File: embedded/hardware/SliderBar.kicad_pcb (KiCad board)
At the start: 2 copper layers, 101.6 x 25.4 mm, 35 parts, among them J1 USB_B_Mini, J2 MOTOR_OUT, J3 POT_IN, J4 DEBUG, U1 MIC5205-3.3YM5, U2 TB6612FNG, U3 MT3608, U4 STM32F072C8Tx

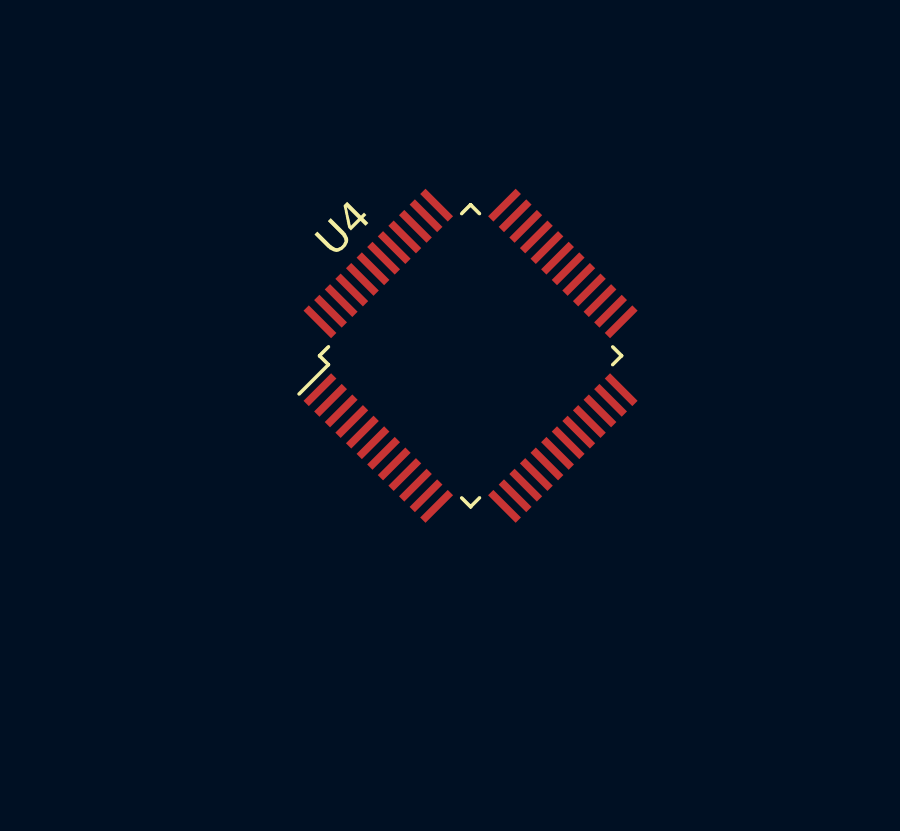
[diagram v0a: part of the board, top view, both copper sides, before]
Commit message: Rotated mcu
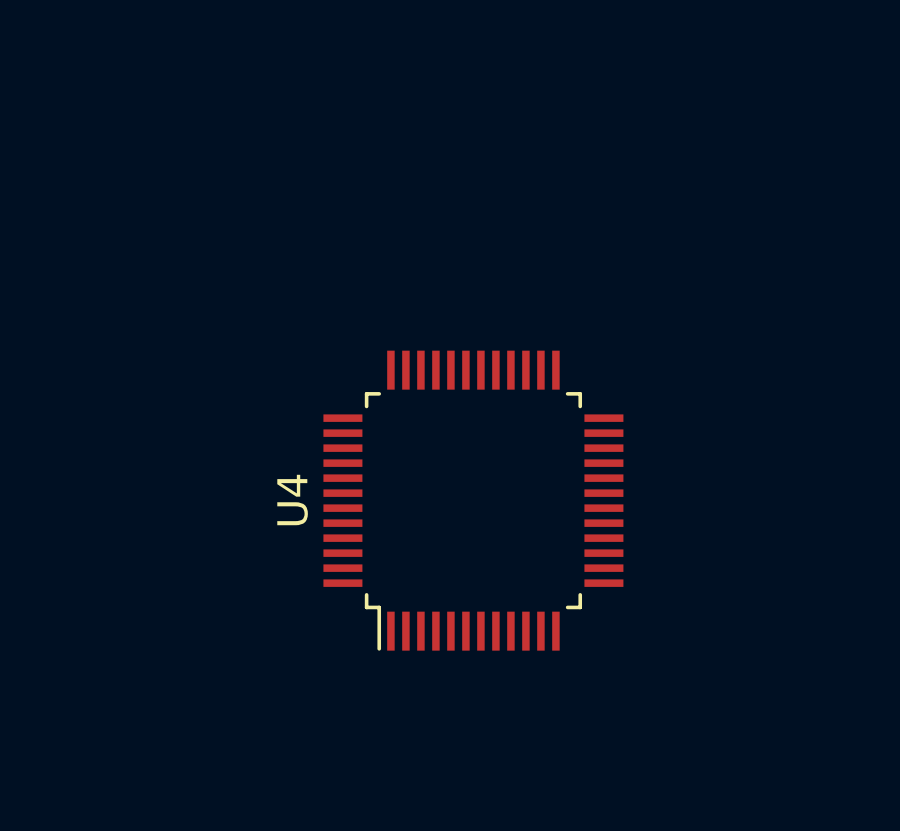
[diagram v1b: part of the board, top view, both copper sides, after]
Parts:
- moved U4 4.83 mm to (120.0, 62.2), turned to 90 degrees

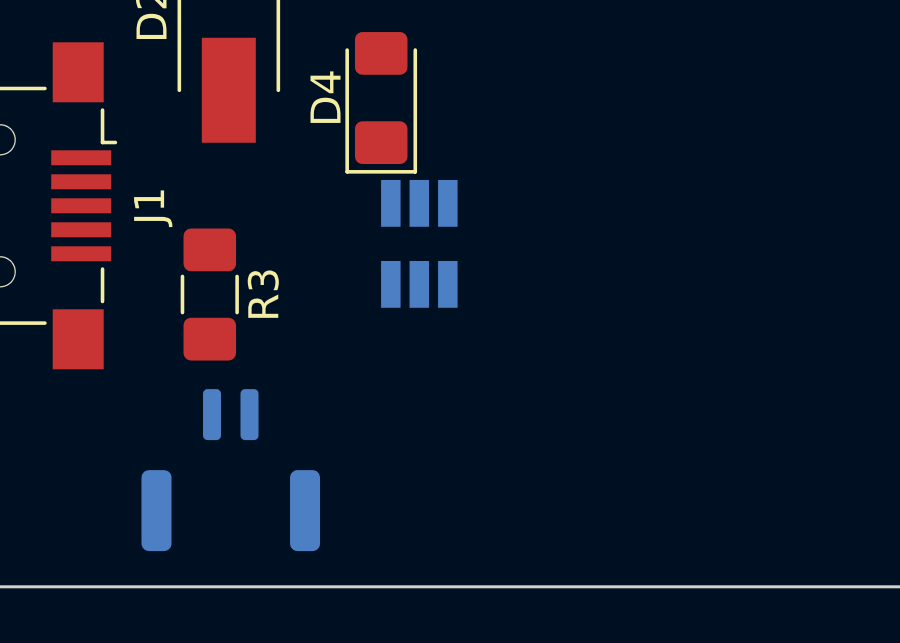
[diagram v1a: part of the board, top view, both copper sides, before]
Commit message: Add GND to power class
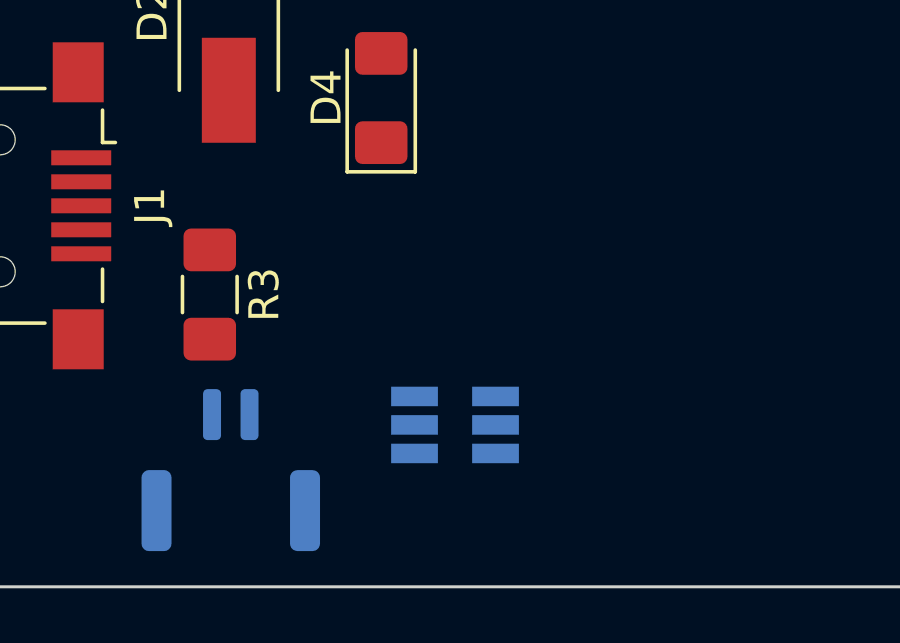
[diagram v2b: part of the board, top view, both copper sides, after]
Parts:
- moved U3 6.15 mm to (115.5, 103.8), turned to 0 degrees
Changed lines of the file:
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@@
     (uvia_drill 0.1)
     (add_net +3V3)
-    (add_net GND)
     (add_net MOT_IN_1)
     (add_net MOT_IN_2)
@@
     (add_net +10V)
     (add_net +5V)
+    (add_net GND)
     (add_net MOT_OUT_1)
     (add_net MOT_OUT_2)
@@
   )
   (module Package_TO_SOT_SMD:SOT-23-6_Handsoldering (layer B.Cu)
-    (at 114.3 97.79 90)
+    (at 115.49 103.825)
     (descr "6-pin SOT-23 package, Handsoldering")
     (tags "SOT-23-6 Handsoldering")
     (attr smd)
-    (fp_text reference U3 (at 0 2.9 90) (layer B.SilkS)
+    (fp_text reference U3 (at 0 2.9) (layer B.SilkS)
       (effects (font (size 1 1) (thickness 0.15)) (justify mirror))
     )
-    (fp_text value MT3608 (at 0 -2.9 90) (layer B.Fab)
+    (fp_text value MT3608 (at 0 -2.9) (layer B.Fab)
       (effects (font (size 1 1) (thickness 0.15)) (justify mirror))
     )
@@
     (fp_line (start 0.9 1.61) (end -2.05 1.61) (layer B.SilkS) (width 0.12))
     (fp_line (start -0.9 -1.61) (end 0.9 -1.61) (layer B.SilkS) (width 0.12))
-    (fp_text user %R (at 0 0) (layer B.Fab)
+    (fp_text user %R (at 0 0 -90) (layer B.Fab)
       (effects (font (size 0.5 0.5) (thickness 0.075)) (justify mirror))
     )
-    (pad 5 smd rect (at 1.35 0 90) (size 1.56 0.65) (layers B.Cu B.Paste B.Mask)
+    (pad 5 smd rect (at 1.35 0) (size 1.56 0.65) (layers B.Cu B.Paste B.Mask)
       (net 2 +5V))
-    (pad 6 smd rect (at 1.35 0.95 90) (size 1.56 0.65) (layers B.Cu B.Paste B.Mask))
-    (pad 4 smd rect (at 1.35 -0.95 90) (size 1.56 0.65) (layers B.Cu B.Paste B.Mask)
+    (pad 6 smd rect (at 1.35 0.95) (size 1.56 0.65) (layers B.Cu B.Paste B.Mask))
+    (pad 4 smd rect (at 1.35 -0.95) (size 1.56 0.65) (layers B.Cu B.Paste B.Mask)
       (net 2 +5V))
-    (pad 3 smd rect (at -1.35 -0.95 90) (size 1.56 0.65) (layers B.Cu B.Paste B.Mask)
+    (pad 3 smd rect (at -1.35 -0.95) (size 1.56 0.65) (layers B.Cu B.Paste B.Mask)
       (net 19 "Net-(R1-Pad2)"))
-    (pad 2 smd rect (at -1.35 0 90) (size 1.56 0.65) (layers B.Cu B.Paste B.Mask)
-      (net 1 GND))
-    (pad 1 smd rect (at -1.35 0.95 90) (size 1.56 0.65) (layers B.Cu B.Paste B.Mask)
+    (pad 2 smd rect (at -1.35 0) (size 1.56 0.65) (layers B.Cu B.Paste B.Mask)
+      (net 1 GND))
+    (pad 1 smd rect (at -1.35 0.95) (size 1.56 0.65) (layers B.Cu B.Paste B.Mask)
       (net 7 "Net-(D1-Pad2)"))
     (model ${KISYS3DMOD}/Package_TO_SOT_SMD.3dshapes/SOT-23-6.wrl

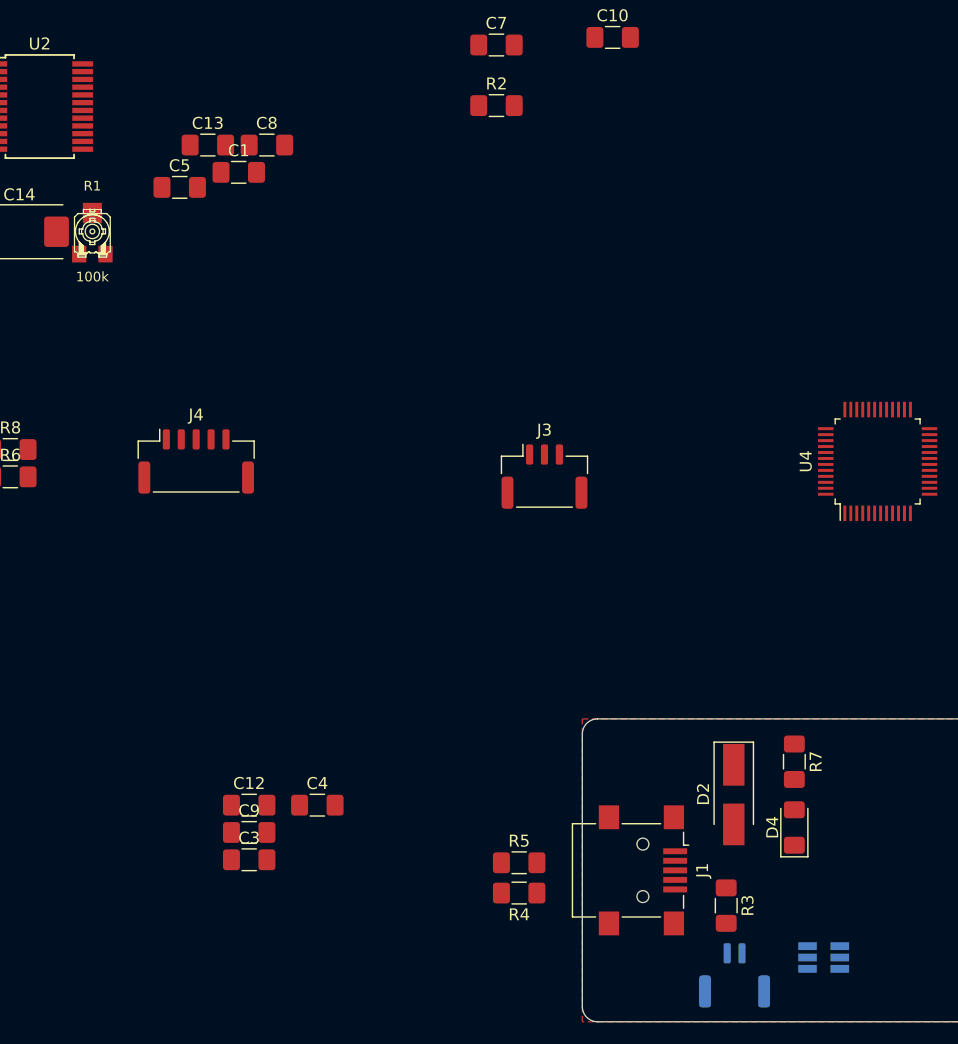
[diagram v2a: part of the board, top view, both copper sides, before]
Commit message: Replace trimpot
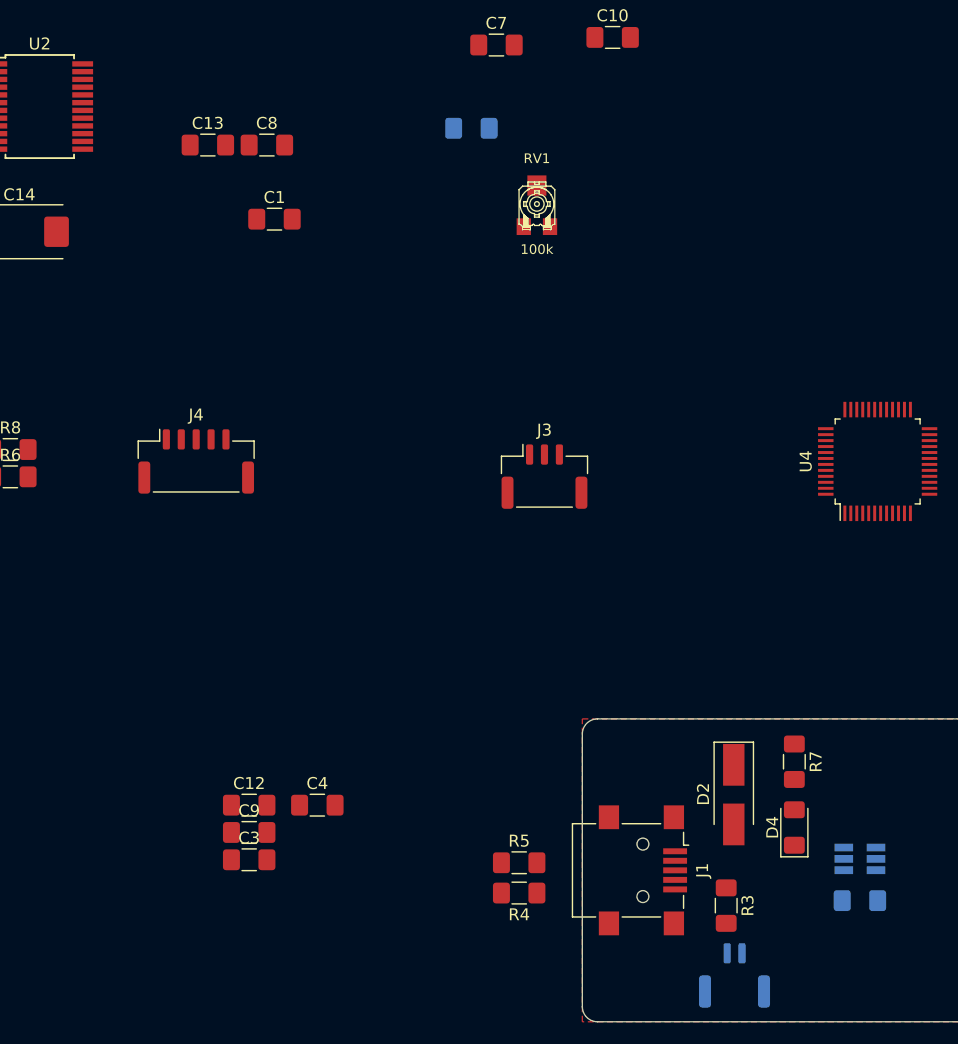
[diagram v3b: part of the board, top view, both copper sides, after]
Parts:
- removed R1: 100k, ab2_passive:AB2_POT_TRIM
- added RV1: 100k, ab2_passive:AB2_POT_TRIM, F.Cu at (91.4, 40.6)
- C5, R2: moved to B.Cu
- moved C5 82.7 mm to (118.5, 99.1)
- moved U3 8.81 mm to (118.5, 95.6), turned to 180 degrees
- moved C1 4.94 mm to (69.4, 41.9)
- moved R2 2.84 mm to (85.9, 34.3)

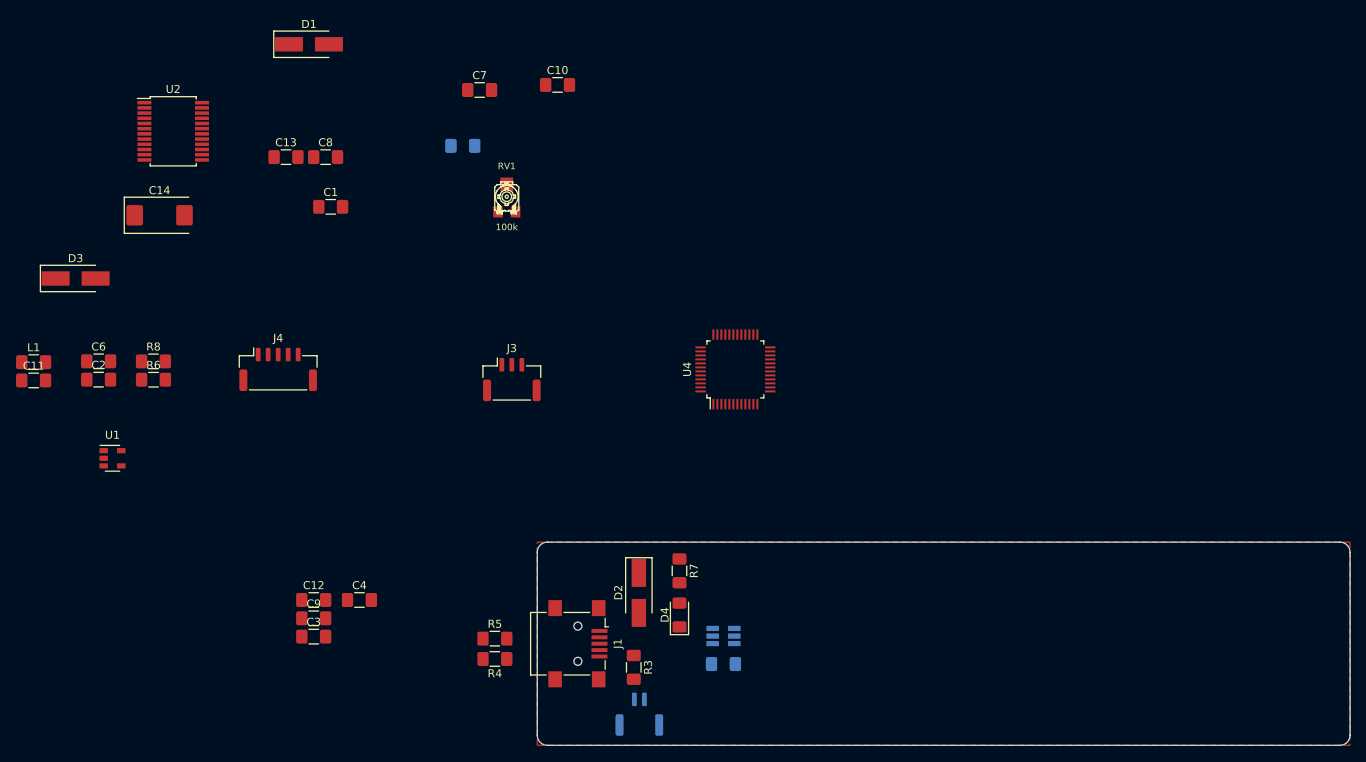
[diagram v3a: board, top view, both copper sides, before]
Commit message: Layout: motor driver, boost converter, 3.3v regulator, debug header, MCU, USB tracks
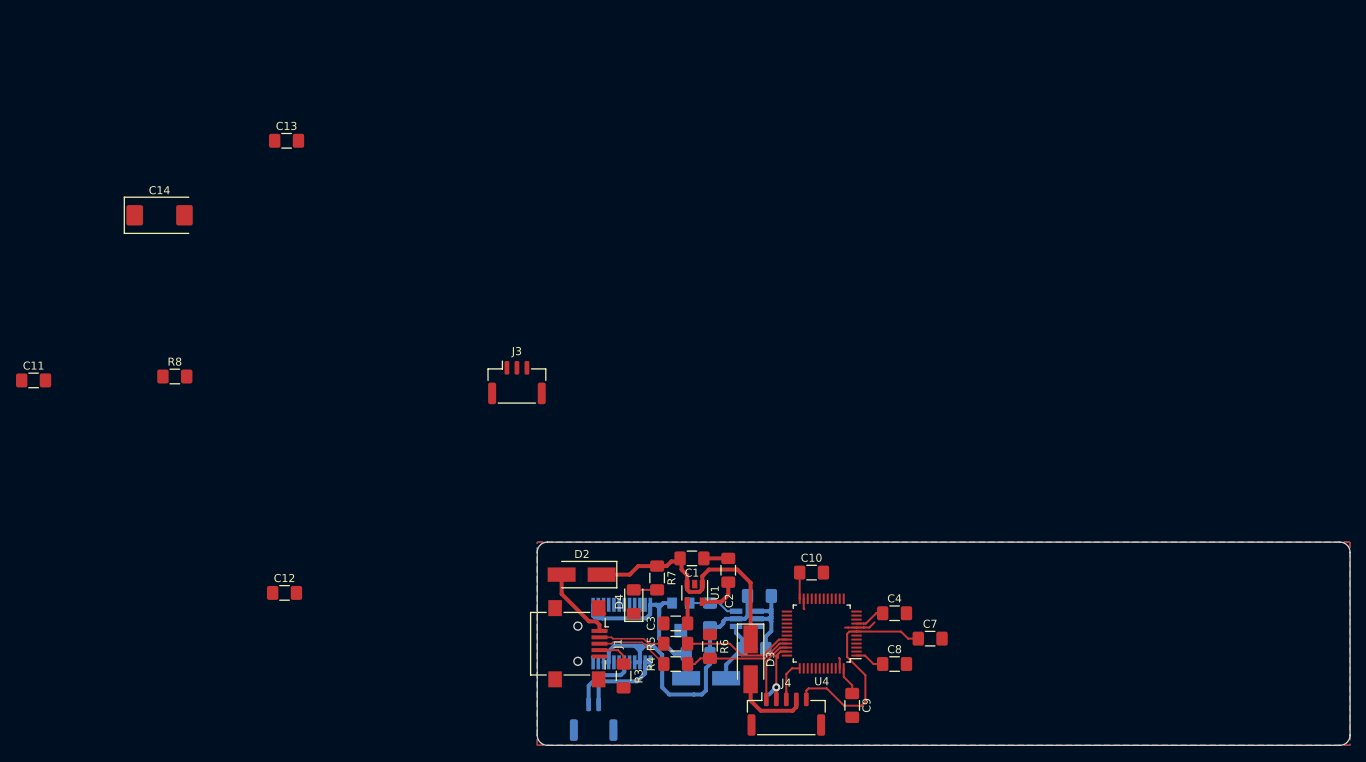
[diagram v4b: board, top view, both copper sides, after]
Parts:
- C6, D1, L1, RV1, U2: moved to B.Cu
- moved L1 96.9 mm to (122.3, 97.2)
- moved D3 96.9 mm to (121.9, 98.5), turned to 270 degrees
- moved C8 95.3 mm to (139.9, 99.1)
- moved D1 93.5 mm to (116.4, 100.8)
- moved C7 88.7 mm to (144.4, 95.9)
- moved U2 84.2 mm to (105.8, 95.2), turned to 90 degrees
- moved C6 83.4 mm to (115.4, 97.8), turned to 180 degrees
- moved C2 82.2 mm to (119.1, 87.3), turned to 90 degrees
- moved R6 77.1 mm to (116.8, 96.9), turned to 270 degrees
- moved J4 76.8 mm to (126.4, 105.3)
- moved U1 74.7 mm to (114.9, 90.2), turned to 270 degrees
- moved C10 68.7 mm to (129.5, 87.6)
- moved C9 68.2 mm to (134.6, 104.2), turned to 270 degrees
- moved C4 66.9 mm to (139.9, 92.7)
- moved R2 66.3 mm to (116.8, 92.9), turned to 90 degrees
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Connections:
- net Net-(J1-Pad2) renamed /D-
- net Net-(J1-Pad3) renamed /D+
- net USB_DM renamed USB_DN
- R2 pad 1: +10V -> GND
- R2 pad 2: GND -> Net-(R2-Pad2)
- RV1 pad 3: Net-(RV1-Pad3) -> Net-(R2-Pad2)
- U3 pad 3: Net-(RV1-Pad3) -> Net-(R2-Pad2)
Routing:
- net GND: track 0.00 -> 61.1 mm, vias 0 -> 1
- net +5V: track 0.00 -> 45.0 mm
- net +10V: track 0.00 -> 28.7 mm
- net NRST: track 0.00 -> 28.5 mm
- net +3V3: track 0.00 -> 19.6 mm
- net USB_DN: track 0.00 -> 13.8 mm
- net USB_DP: track 0.00 -> 13.5 mm
- net MOT_OUT_1: track 0.00 -> 10.9 mm
- net VBUS: track 0.00 -> 10.2 mm
- net VPP: track 0.00 -> 10.1 mm
- net MOT_OUT_2: track 0.00 -> 9.34 mm
- net /D+: track 0.00 -> 9.24 mm
- net /D-: track 0.00 -> 8.37 mm
- net SWDIO: track 0.00 -> 8.05 mm
- net Net-(D1-Pad2): track 0.00 -> 8.01 mm
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- added copper zone on B.Cu, net GND
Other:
- net class Power: clearance 0.13 -> 0.15; trace_width 1 -> 0.5; via_dia 1.6 -> 1; via_drill 0.8 -> 0.5
